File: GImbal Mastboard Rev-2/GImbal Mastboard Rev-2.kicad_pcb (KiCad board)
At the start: 2 copper layers, 26 parts, among them U1 TM4C123G, U2 OKI-5V, U3 IMU-LSM90S1, U4 Raspberry_Pi_Header, U5 TIVA_Rear_Headers, U6 JAG_ARM_Connector-10pin, U7 Molex_SL-4, U8 Molex_SL-3, Y1 16MHz

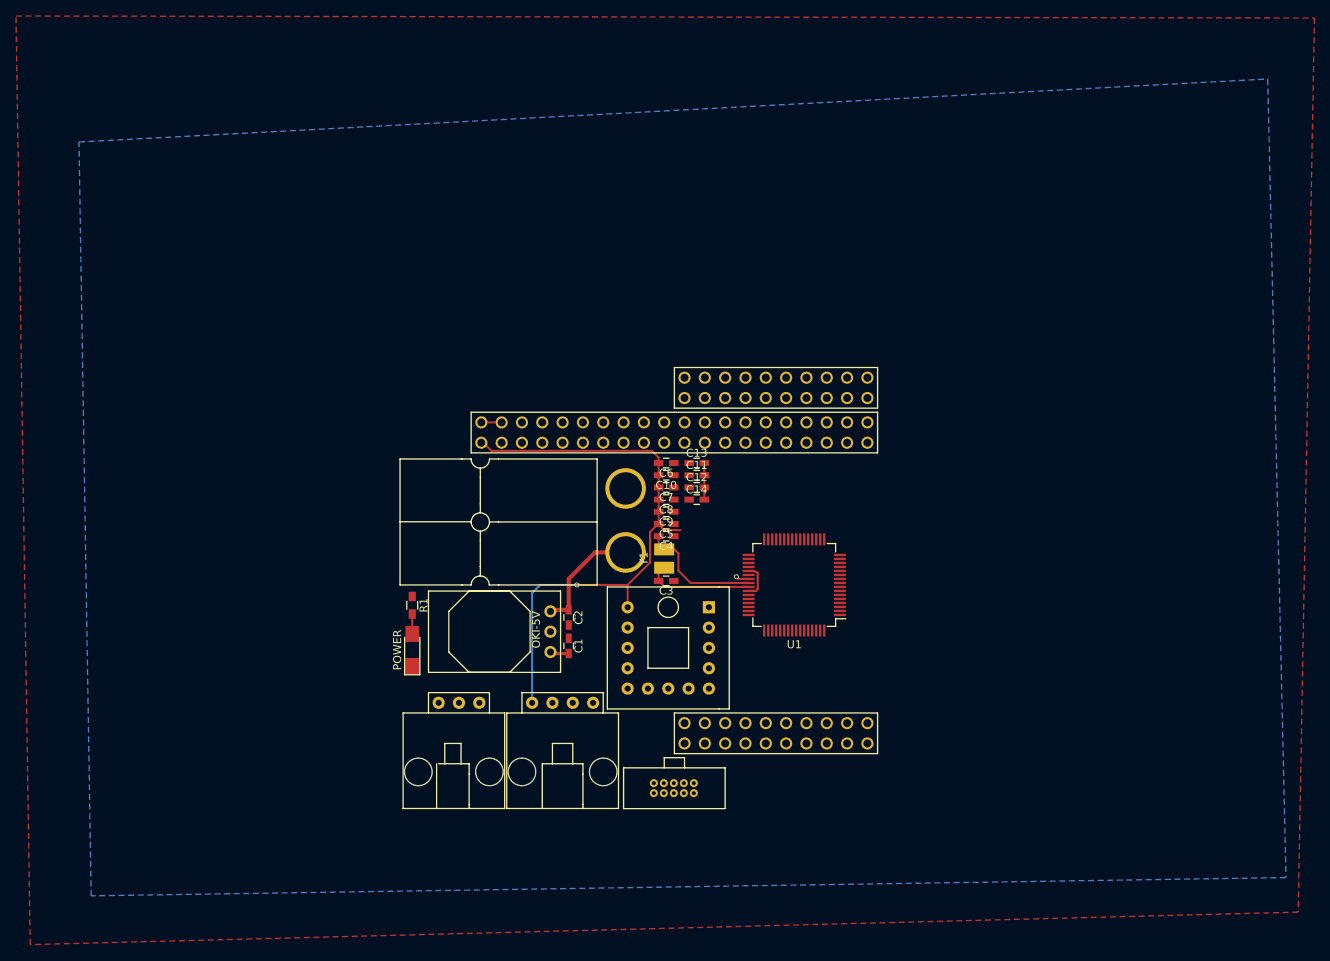
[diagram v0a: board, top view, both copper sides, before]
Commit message: finished board layout
I'll add text and modify silkscren later. I will also try to rout to the TIVA footprint
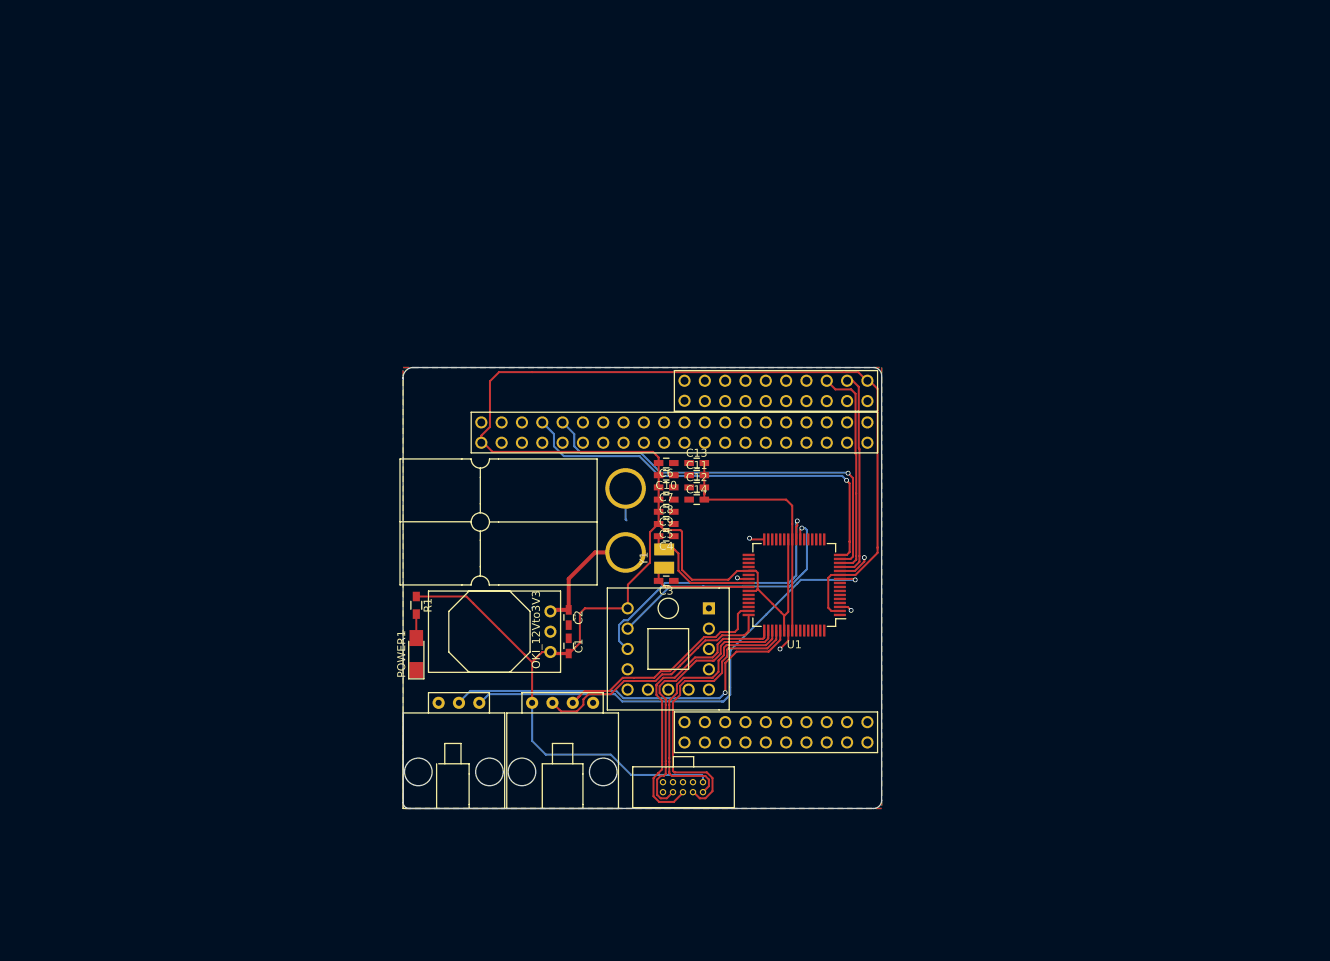
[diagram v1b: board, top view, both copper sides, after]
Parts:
- removed POWER: Green, LEDs:LED_1206_HandSoldering
- added POWER1: Green, LEDs:LED_1206_HandSoldering, F.Cu at (120.7, 126.0)
- U2: value OKI-5V -> OKI_12Vto3V3
- U5: value TIVA_Rear_Headers -> TM4C129E_Rear_Headers; footprint MRDT_KICAD_PACKAGES:TIVA_REAR_HEADERS -> MRDT_KICAD_PACKAGES:TM4C129E_HALF_HEADERS
- moved U6 1.15 mm to (147.7, 140.1)
- moved R1 0.51 mm to (120.7, 119.9)
- moved U5 0.13 mm to (152.9, 138.3)
- moved U3 0.13 mm to (144.5, 133.0)
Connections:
- C1 pad 2: +5V -> +3V3
- R1 pad 1: +5V -> +3V3
- U1 pad 10: PI_RX -> TX_2
- U1 pad 15: TX_4 -> PI_RX
- U1 pad 16: RX_4 -> PI_TX
- U1 pad 53: PI_TX -> RX_2
- U2 pad 3: +5V -> +3V3
- U4 pad 2: +5V -> (no net)
- U4 pad 4: +5V -> (no net)
- U8 pad 1: TX_4 -> TX_2
- U8 pad 2: RX_4 -> RX_2
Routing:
- net +3V3: track 77.3 -> 242.9 mm, vias 1 -> 0
- net TX_2: track 0.00 -> 59.3 mm, vias 0 -> 1
- net PI_TX: track 0.00 -> 52.5 mm, vias 0 -> 1
- net PI_RX: track 0.00 -> 51.8 mm, vias 0 -> 1
- net RX_2: track 0.00 -> 47.6 mm, vias 0 -> 1
- net SDA_1: track 0.00 -> 38.1 mm, vias 0 -> 1
- net TCK: track 0.00 -> 38.0 mm
- net TDO: track 0.00 -> 36.8 mm
- net TMS: track 0.00 -> 35.4 mm
- net TDI: track 0.00 -> 34.7 mm
- net SCL_1: track 0.00 -> 32.6 mm, vias 0 -> 1
- net SDA_0: track 0.00 -> 31.6 mm
- net SCL_0: track 0.00 -> 28.2 mm
- net RX_3: track 0.00 -> 27.3 mm
- net Net-(C11-Pad2): track 4.57 -> 31.6 mm
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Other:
- board outline added: 59.8 x 55.1 mm
- net class Default: clearance 0.2 -> 0.15
- rule trace_clearance: 0.2 -> 0.15

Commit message: Finished Board Wiring
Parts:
- added JP1: Jumper, Pin_Headers:Pin_Header_Straight_1x02_Pitch2.54mm, F.Cu at (164.7, 140.5)
- added JP2: Jumper, Pin_Headers:Pin_Header_Straight_1x02_Pitch2.54mm, F.Cu at (162.2, 143.0)
- added JP3: Jumper_NC_Dual, Pin_Headers:Pin_Header_Straight_1x03_Pitch1.27mm, F.Cu at (137.7, 94.1)
- added JP4: Jumper_NC_Dual, Pin_Headers:Pin_Header_Straight_1x03_Pitch1.27mm, F.Cu at (137.7, 91.9)
- U5: value TM4C129E_Rear_Headers -> TIVA_C_TM4C123_Launchpad_Shield; footprint MRDT_KICAD_PACKAGES:TM4C129E_HALF_HEADERS -> MRDT_KICAD_PACKAGES:TM4C123G_Booster
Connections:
- net RX_2 renamed PD6
- net TX_2 renamed PD7
- U1 pad 1: (no net) -> PB6
- U1 pad 13: TIVA_RX -> PC7
- U1 pad 14: RX_3 -> PC6
- U1 pad 15: PI_RX -> PC5
- U1 pad 16: PI_TX -> PC4
- U1 pad 19: (no net) -> PA2
- U1 pad 20: (no net) -> PA3
- U1 pad 21: (no net) -> PA4
- U1 pad 22: (no net) -> PA5
- U1 pad 23: SCL_1 -> PA6
- U1 pad 24: SDA_1 -> PA7
- U1 pad 28: (no net) -> PF0
- U1 pad 29: (no net) -> PF1
- U1 pad 30: (no net) -> PF2
- U1 pad 31: (no net) -> PF3
- U1 pad 4: (no net) -> PB7
- U1 pad 43: (no net) -> PD4
- U1 pad 44: (no net) -> PD5
- U1 pad 45: (no net) -> PB0
- U1 pad 46: (no net) -> PB1
- U1 pad 47: SCL_0 -> PB2
- U1 pad 48: SDA_0 -> PB3
- U1 pad 5: (no net) -> PF4
- U1 pad 57: (no net) -> PB5
- U1 pad 58: (no net) -> PB4
- U1 pad 59: (no net) -> IMU_SCL
- U1 pad 6: (no net) -> PE3
- U1 pad 60: (no net) -> IMU_SDA
- U1 pad 61: (no net) -> PD0
- U1 pad 62: (no net) -> PD1
- U1 pad 63: (no net) -> PD2
- U1 pad 64: (no net) -> PD3
- U1 pad 7: (no net) -> PE2
- U1 pad 8: (no net) -> PE1
- U1 pad 9: (no net) -> PE0
- U3 pad 2: SCL_1 -> IMU_SCL
- U3 pad 3: SDA_1 -> IMU_SDA
- U7 pad 2: SCL_0 -> PA6
- U7 pad 3: SDA_0 -> PA7
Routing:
- net PA7: track 0.00 -> 85.3 mm
- net PA6: track 0.00 -> 74.7 mm
- net PD5: track 0.00 -> 54.2 mm, vias 0 -> 1
- net PC5: track 0.00 -> 52.9 mm
- net PC4: track 0.00 -> 51.5 mm
- net PD4: track 0.00 -> 51.1 mm, vias 0 -> 2
- net PE0: track 0.00 -> 49.2 mm
- net PI_TX: track 52.5 -> 4.62 mm, vias 1 -> 0
- net +3V3: track 242.9 -> 196.8 mm, vias 0 -> 5
- net PI_RX: track 51.8 -> 7.62 mm, vias 1 -> 0
- net PB6: track 0.00 -> 39.6 mm, vias 0 -> 1
- net PF1: track 0.00 -> 39.2 mm, vias 0 -> 3
- net PB7: track 0.00 -> 39.0 mm, vias 0 -> 1
- net SDA_1: track 38.1 -> 0.00 mm, vias 1 -> 0
- net PB2: track 0.00 -> 33.2 mm, vias 0 -> 1
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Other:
- net class Default: clearance 0.15 -> 0.12192; via_dia 0.6 -> 0.5
- rule trace_clearance: 0.15 -> 0.12192

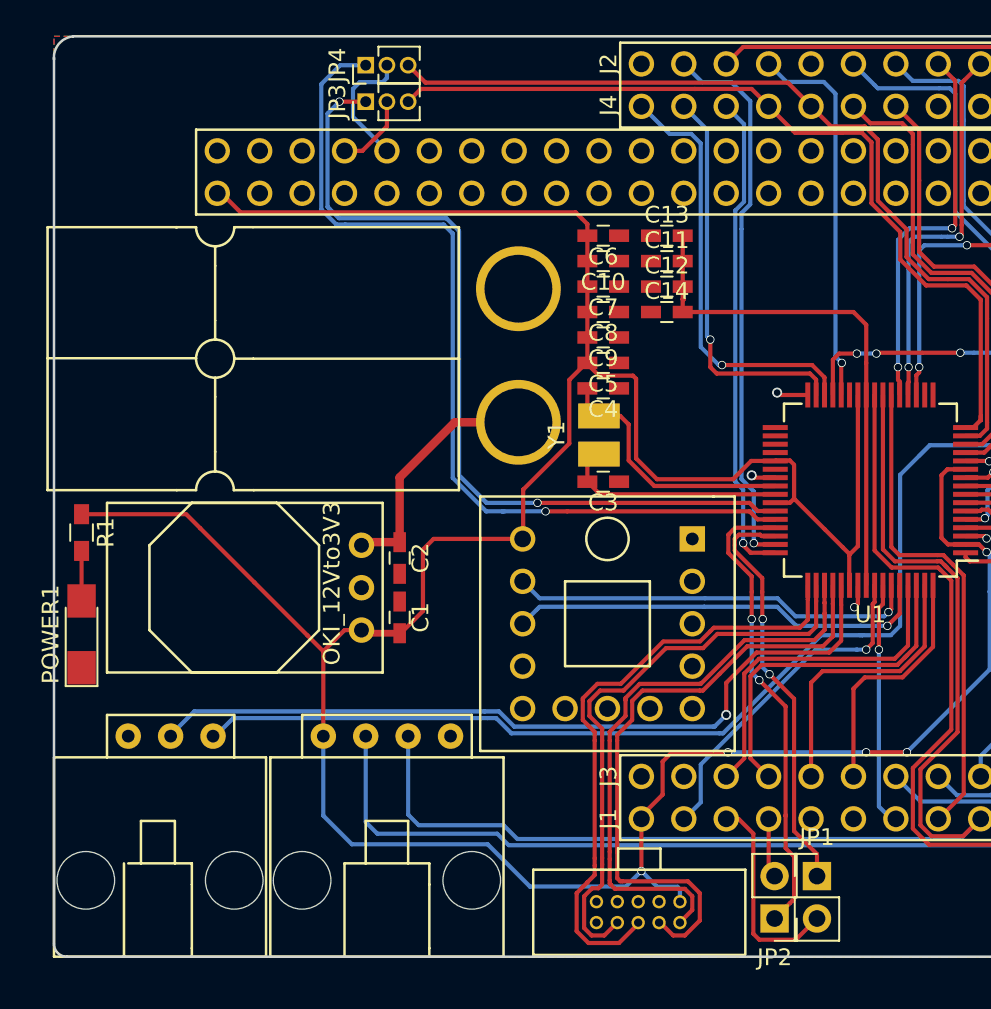
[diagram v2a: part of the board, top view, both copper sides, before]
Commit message: Modified silkscreen
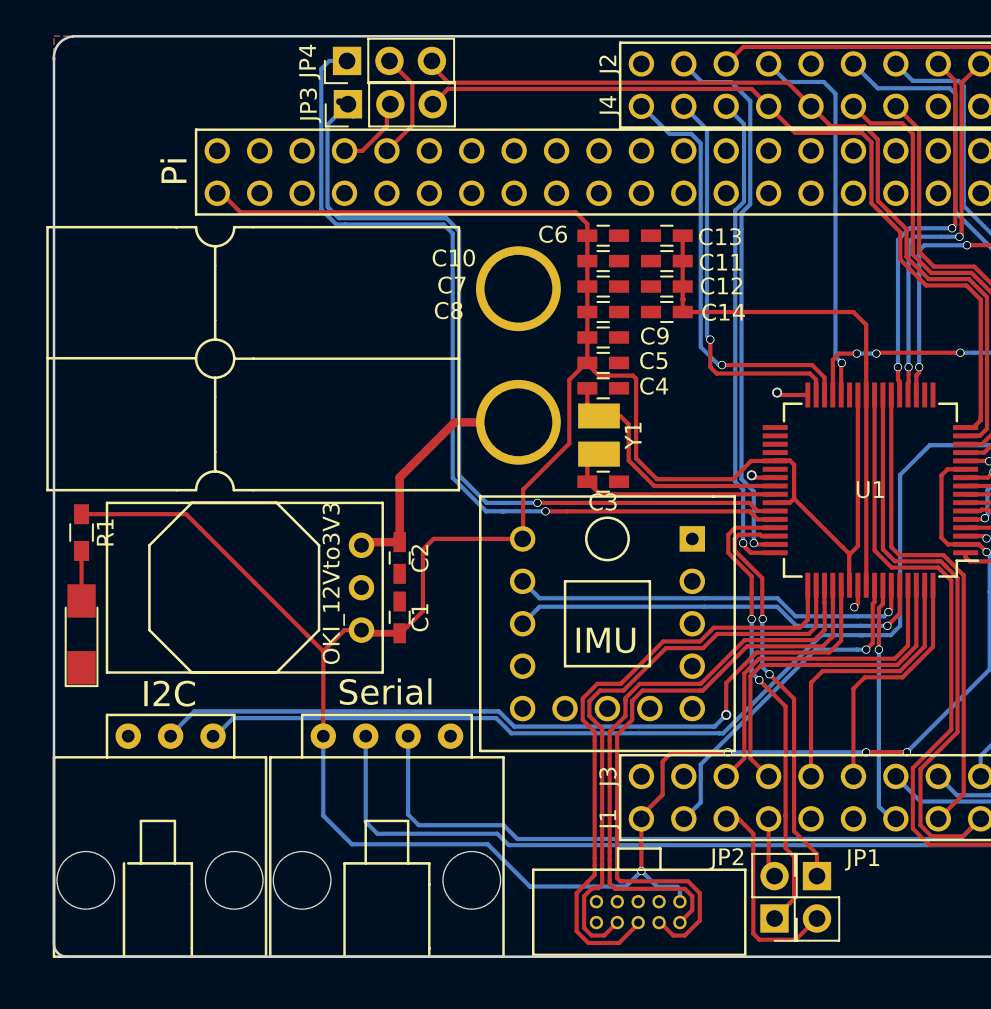
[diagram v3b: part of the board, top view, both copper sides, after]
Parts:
- JP3, JP4: footprint Pin_Headers:Pin_Header_Straight_1x03_Pitch1.27mm -> Pin_Headers:Pin_Header_Straight_1x03_Pitch2.54mm
- moved JP4 1.15 mm to (136.6, 91.6)
- moved JP3 1.08 mm to (136.6, 94.2)
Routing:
- net PC4: track 51.5 -> 50.1 mm
- net PC5: track 52.9 -> 51.8 mm
- net PI_RX: track 7.62 -> 6.58 mm
- net PD4: track 51.1 -> 50.4 mm
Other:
- board text added: "I2C"
- board text added: "IMU"
- board text added: "Mast Board Missouri S&T Mars Rover, 2018 Andrew Van Horn"
- board text added: "Pi"
- board text added: "Serial"

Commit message: Modified board
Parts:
- U8: footprint MRDT_KICAD_PACKAGES:MOLEX_SL_3 -> MRDT-Connectors:MOLEX_SL_3
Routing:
- net PB1: track 24.8 -> 26.5 mm
- net PD6: track 47.8 -> 48.3 mm
- net PC4: track 50.1 -> 50.6 mm
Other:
- net class Default: clearance 0.12192 -> 0.14224
- rule trace_clearance: 0.12192 -> 0.14224

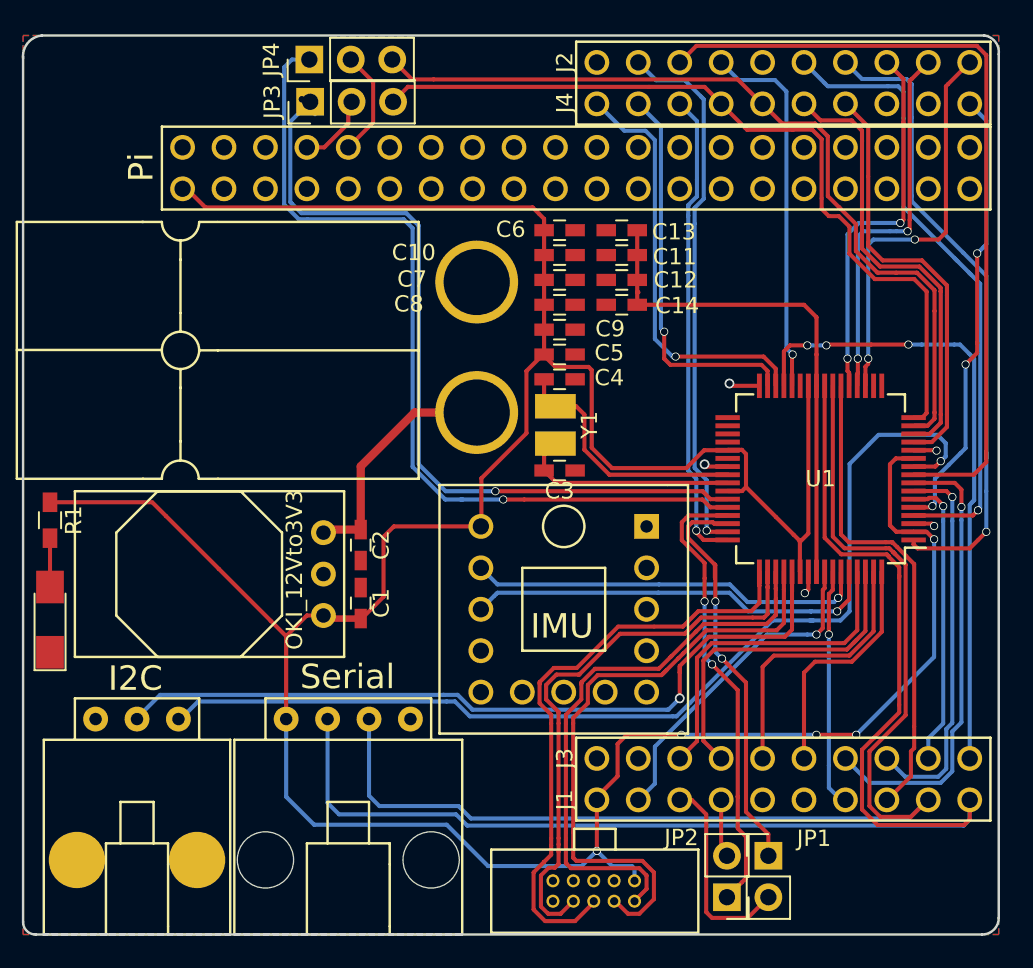
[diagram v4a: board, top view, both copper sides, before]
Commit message: Added PWM Output on Headers as backup if serial does not work.
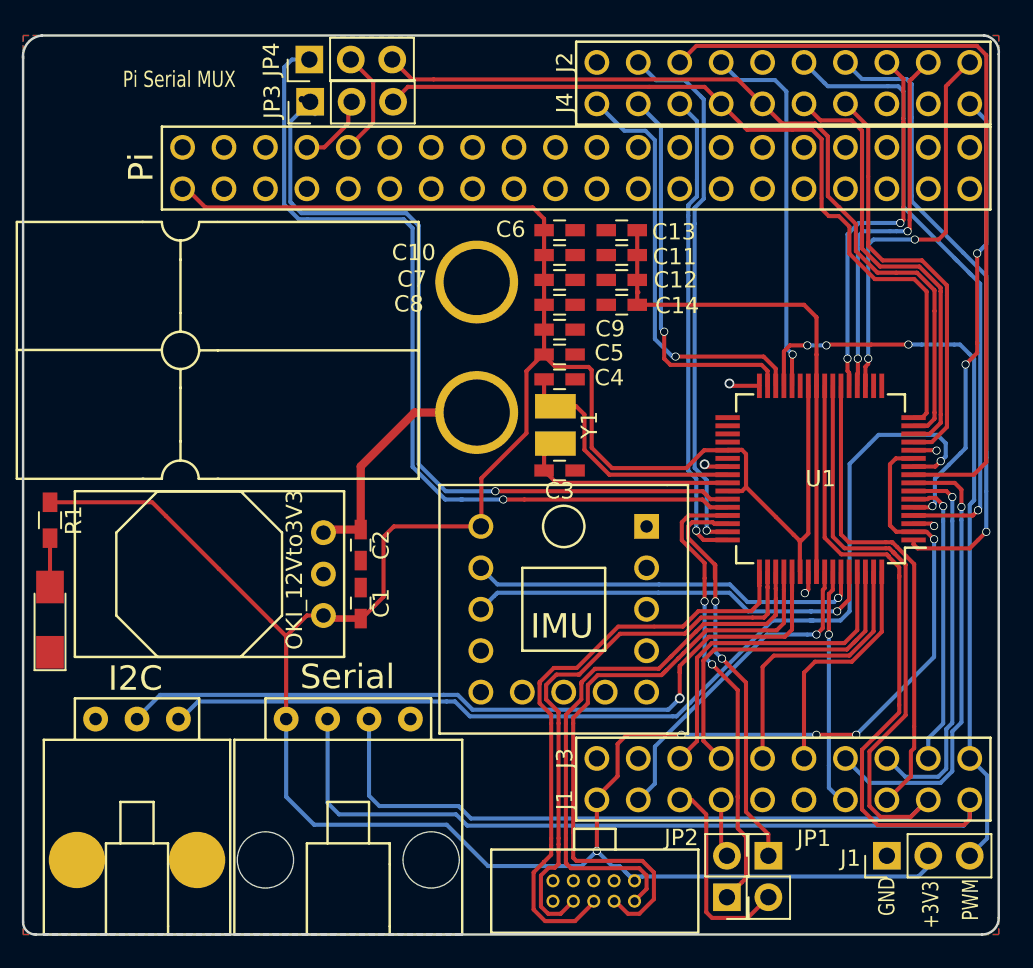
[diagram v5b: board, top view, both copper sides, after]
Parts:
- added J1: Conn_01x03_Female, Socket_Strips:Socket_Strip_Straight_1x03_Pitch2.54mm, F.Cu at (172.0, 140.5)
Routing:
- net +3V3: track 196.6 -> 215.7 mm
- net PF1: track 39.2 -> 46.0 mm
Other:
- board text added: "+3V3"
- board text added: "GND"
- board text added: "PWM"
- board text added: "Pi Serial MUX"
